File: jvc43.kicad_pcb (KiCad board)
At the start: 6 copper layers, 101.6 x 50.8 mm, 134 parts, among them J201 8P8C_LED_Shielded, J301 8P8C_LED_Shielded, J401 USB_C_Receptacle_USB2.0, U201 LAN8831, U301 LAN8831, U401 LTC3622*DE, X101 25 MHz

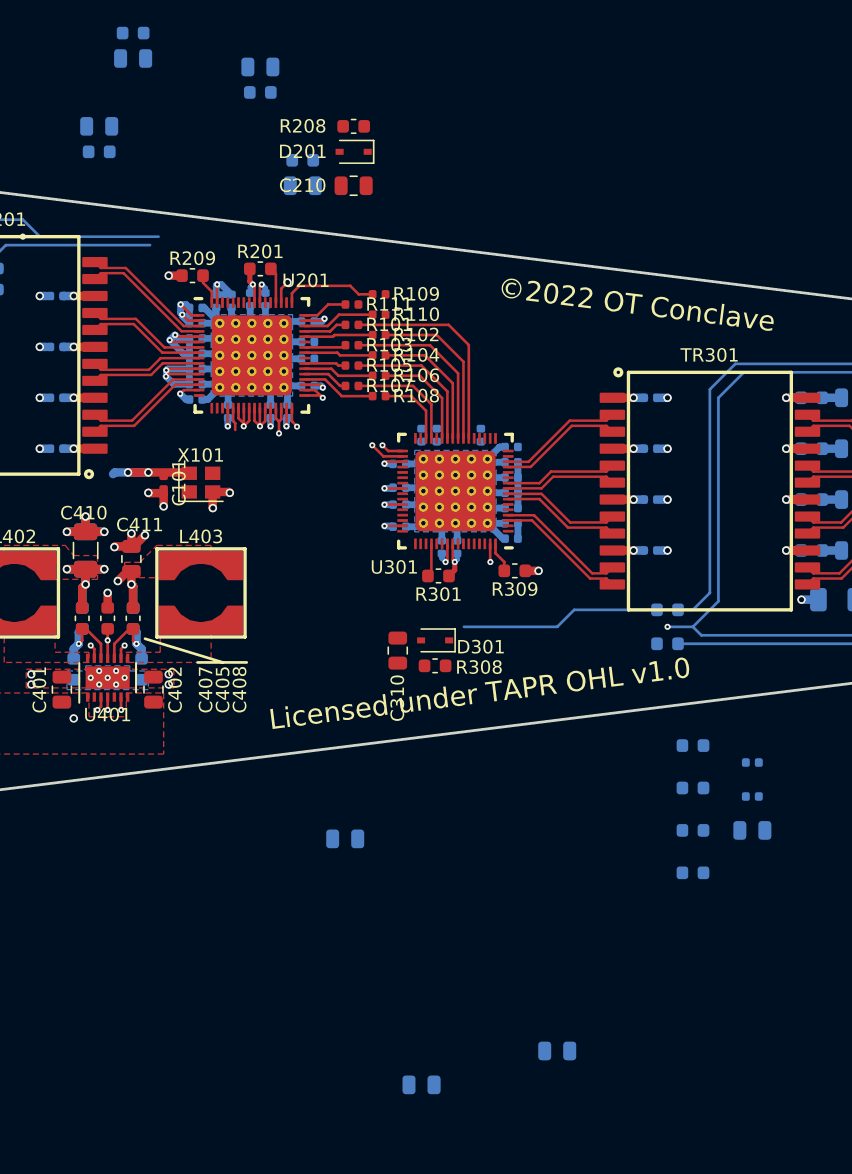
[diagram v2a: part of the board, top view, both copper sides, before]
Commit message: Routed the entire rest of the PHY1/2 bypass caps, inductors, and local power planes.  Had to move the oscillator to the right a bit to make way.
Also added a 50mil board edge keepout for components on the drawings layer.
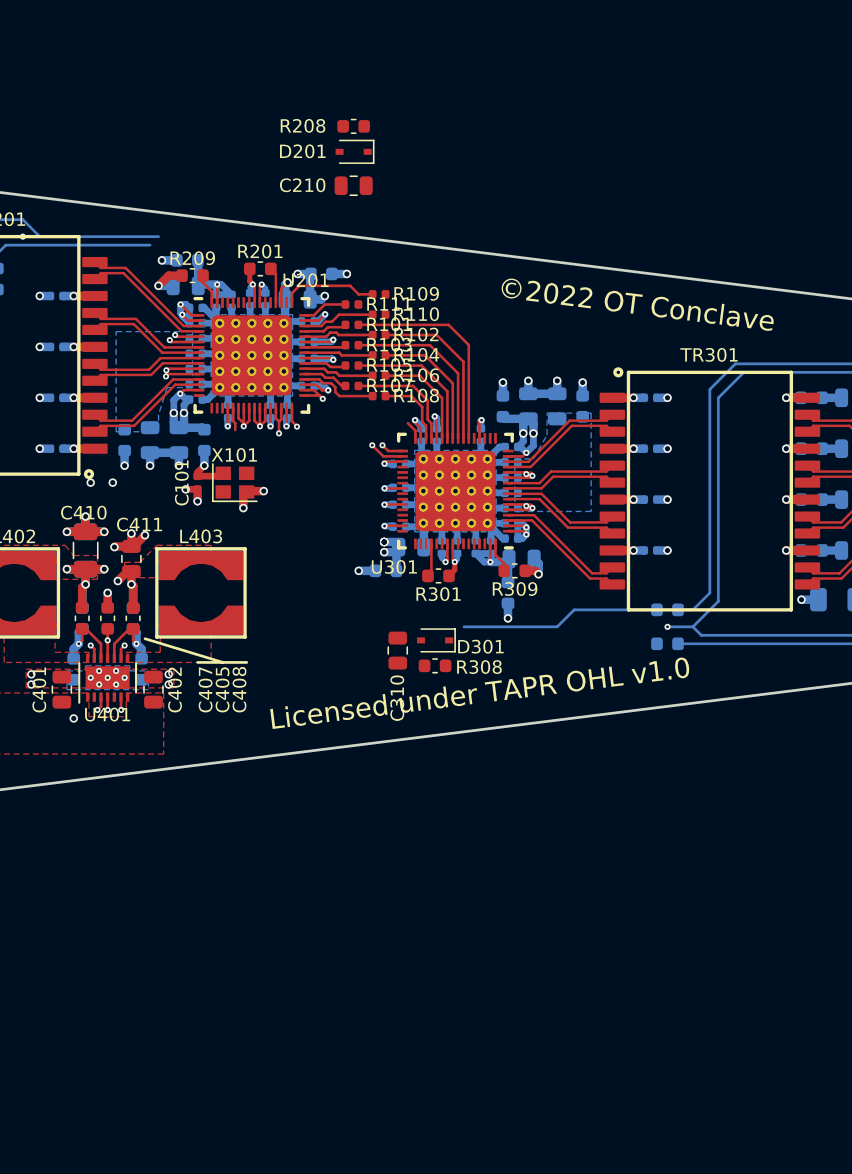
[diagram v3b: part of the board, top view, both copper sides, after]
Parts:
- moved C329 48.3 mm to (91.4, 44.5), turned to 90 degrees
- moved C319 40.3 mm to (80.5, 55.0)
- moved L301 37.7 mm to (87.4, 44.5), turned to 270 degrees
- moved C311 35.2 mm to (89.3, 44.5), turned to 90 degrees
- moved L303 32.8 mm to (93.3, 44.5), turned to 90 degrees
- moved L201 30.9 mm to (65.0, 47.0), turned to 90 degrees
- moved C211 28.8 mm to (63.1, 47.0), turned to 270 degrees
- moved C331 27.9 mm to (85.3, 55.0), turned to 90 degrees
- moved C332 26.7 mm to (88.8, 55.9)
- moved L302 26.4 mm to (78.6, 56.8), turned to 180 degrees
- moved C330 25.4 mm to (86.5, 55.0), turned to 90 degrees
- moved C229 23.8 mm to (61.0, 47.0), turned to 270 degrees
- moved L203 21.7 mm to (59.1, 47.0), turned to 270 degrees
- moved L304 20.1 mm to (87.8, 58.4), turned to 270 degrees
- moved C232 17.3 mm to (63.6, 35.4), turned to 180 degrees
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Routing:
- net GND: track 194.1 -> 214.3 mm, vias 45 -> 49
- net /Ethernet2/VDDAH: track 1.14 -> 15.9 mm, vias 0 -> 5
- net /Ethernet1/VDDAL: track 20.4 -> 9.15 mm
- net /Ethernet1/VDD: track 6.29 -> 15.1 mm, vias 3 -> 6
- net /Ethernet1/VDDAH: track 9.12 -> 16.4 mm, vias 3 -> 5
- net /Ethernet2/VDD: track 6.22 -> 13.3 mm, vias 3 -> 8
- net +1V1: track 11.6 -> 18.3 mm, vias 3 -> 9
- net /Ethernet2/VDDAL_PLL: track 1.37 -> 7.80 mm
- net +2V5: track 30.4 -> 36.7 mm, vias 11 -> 16
- net /Ethernet2/VDDAL: track 3.43 -> 7.81 mm, vias 0 -> 4
- net /Ethernet1/VDDAL_PLL: track 4.68 -> 8.06 mm
- net /ER_W2B: track 0.00 -> 1.36 mm
- added copper zone on L4.Cu, net /Ethernet1/VDD
- added copper zone on L4.Cu, net /Ethernet1/VDDAH
- added copper zone on B.Cu, net /Ethernet1/VDDAL
- added copper zone on L4.Cu, net /Ethernet2/VDD
- added copper zone on L4.Cu, net /Ethernet2/VDDAH
- added copper zone on B.Cu, net /Ethernet2/VDDAL

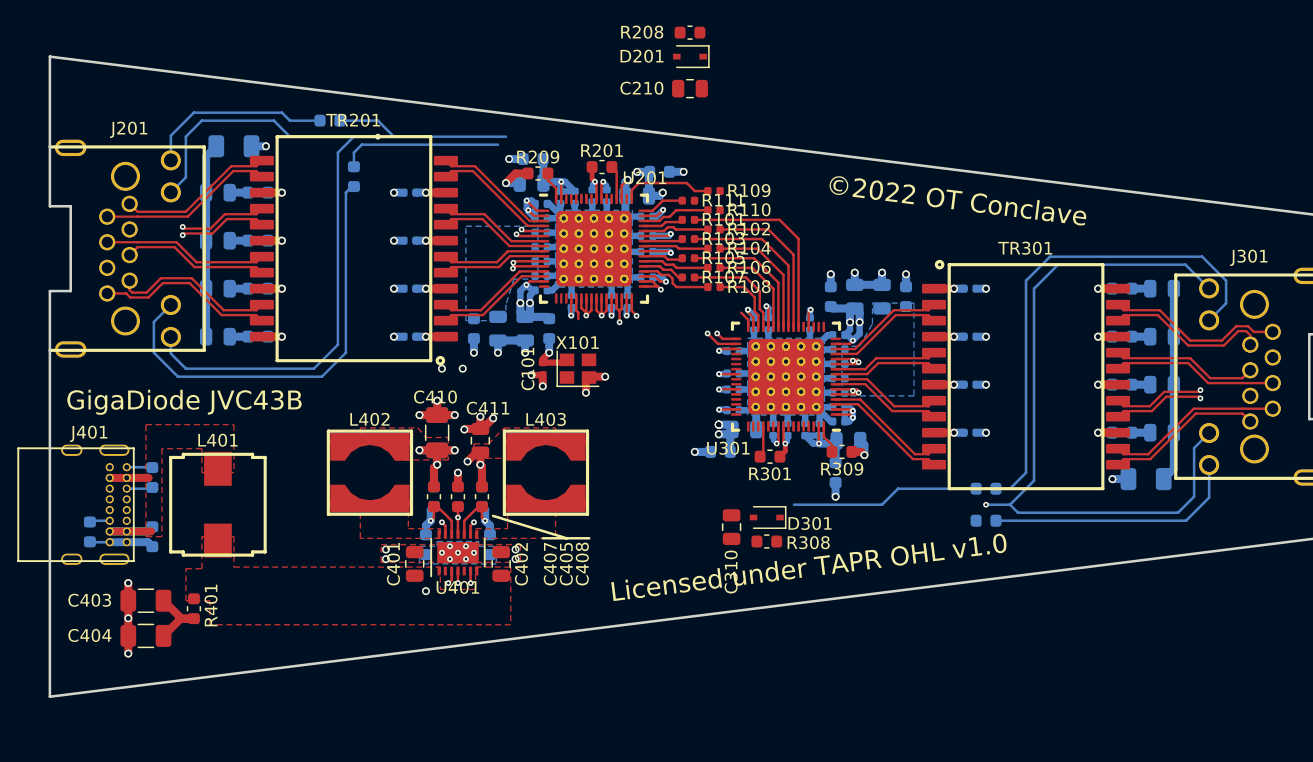
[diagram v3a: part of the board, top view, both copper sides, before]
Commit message: - Tweaked polygon shape of the two VDDAH slightly - Added fiducials (at the layout level, rather than schematic)
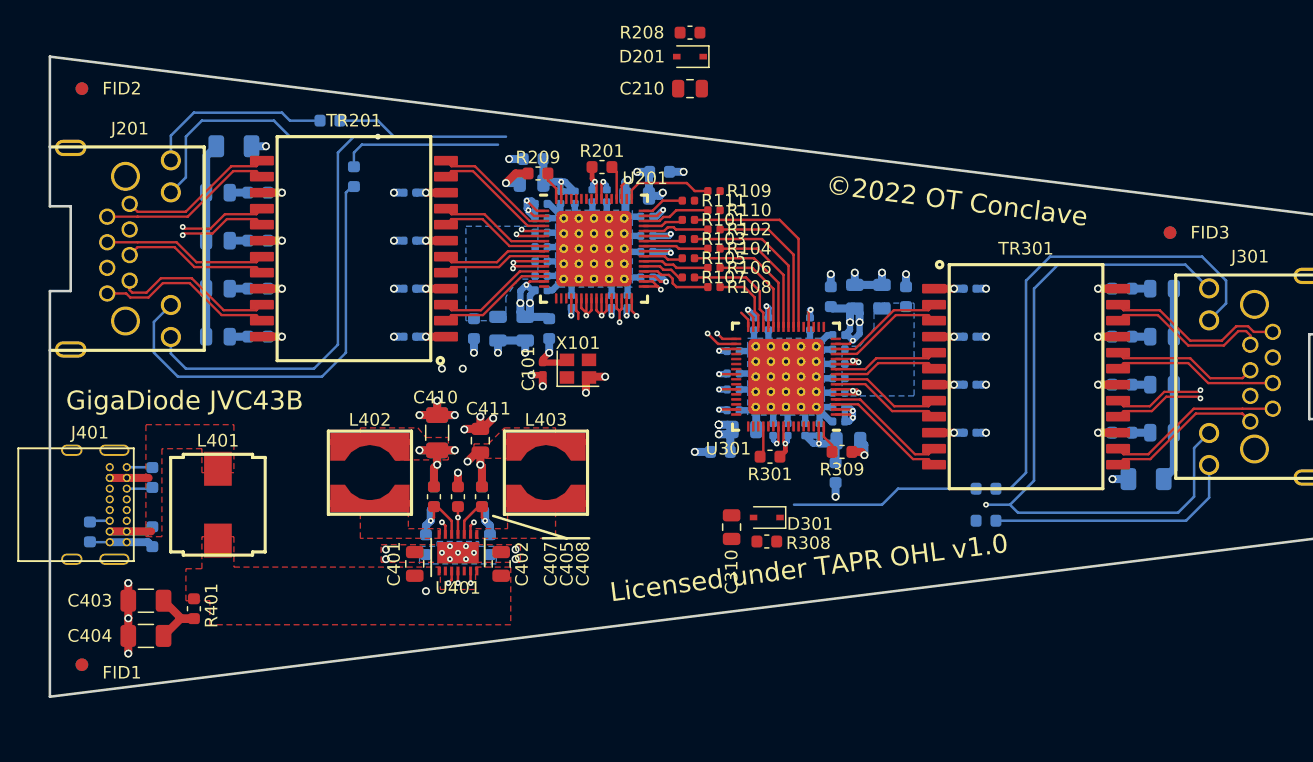
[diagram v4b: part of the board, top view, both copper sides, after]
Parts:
- added FID1: Fiducial_1mm_Dia_2mm_Outer, Fiducial:Fiducial_1mm_Dia_2mm_Outer, F.Cu at (27.9, 73.7)
- added FID2: Fiducial_1mm_Dia_2mm_Outer, Fiducial:Fiducial_1mm_Dia_2mm_Outer, F.Cu at (27.9, 27.9)
- added FID3: Fiducial_1mm_Dia_2mm_Outer, Fiducial:Fiducial_1mm_Dia_2mm_Outer, F.Cu at (114.3, 39.4)
- added FID4: Fiducial_1mm_Dia_2mm_Outer, Fiducial:Fiducial_1mm_Dia_2mm_Outer, B.Cu at (27.9, 73.7)
- added FID5: Fiducial_1mm_Dia_2mm_Outer, Fiducial:Fiducial_1mm_Dia_2mm_Outer, B.Cu at (27.9, 27.9)
- added FID6: Fiducial_1mm_Dia_2mm_Outer, Fiducial:Fiducial_1mm_Dia_2mm_Outer, B.Cu at (114.3, 39.4)
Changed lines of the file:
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@@
     (tracks 926)
     (zones 0)
-    (modules 134)
+    (modules 140)
     (nets 163)
   )
@@
     )
   )
+  (module Fiducial:Fiducial_1mm_Dia_2mm_Outer locked (layer F.Cu)
+    (at 27.94 73.66)
+    (descr "Circular Fiducial, 1mm bare copper top, 2mm keepout (Level A)")
+    (tags fiducial)
+    (attr smd)
+    (fp_text reference FID1 (at 3.175 0.635) (layer F.SilkS)
+      (effects (font (size 1 1) (thickness 0.15)))
+    )
+    (fp_text value Fiducial_1mm_Dia_2mm_Outer (at 0 2) (layer F.Fab)
+      (effects (font (size 1 1) (thickness 0.15)))
+    )
+    (fp_circle (center 0 0) (end 1.25 0) (layer F.CrtYd) (width 0.05))
+    (fp_text user %R (at 0 0) (layer F.Fab)
+      (effects (font (size 0.4 0.4) (thickness 0.06)))
+    )
+    (fp_circle (center 0 0) (end 1 0) (layer F.Fab) (width 0.1))
+    (pad "" smd circle (at 0 0) (size 1 1) (layers F.Cu F.Mask)
+      (solder_mask_margin 0.5) (clearance 0.5))
+  )
+  (module Fiducial:Fiducial_1mm_Dia_2mm_Outer locked (layer B.Cu)
+    (at 27.94 73.66)
+    (descr "Circular Fiducial, 1mm bare copper top, 2mm keepout (Level A)")
+    (tags fiducial)
+    (attr smd)
+    (fp_text reference FID4 (at 0 -1.905) (layer B.SilkS)
+      (effects (font (size 1 1) (thickness 0.15)) (justify mirror))
+    )
+    (fp_text value Fiducial_1mm_Dia_2mm_Outer (at 0 -2) (layer B.Fab)
+      (effects (font (size 1 1) (thickness 0.15)) (justify mirror))
+    )
+    (fp_circle (center 0 0) (end 1.25 0) (layer B.CrtYd) (width 0.05))
+    (fp_text user %R (at 0 0) (layer B.Fab)
+      (effects (font (size 0.4 0.4) (thickness 0.06)) (justify mirror))
+    )
+    (fp_circle (center 0 0) (end 1 0) (layer B.Fab) (width 0.1))
+    (pad "" smd circle (at 0 0) (size 1 1) (layers B.Cu B.Mask)
+      (solder_mask_margin 0.5) (clearance 0.5))
+  )
+  (module Fiducial:Fiducial_1mm_Dia_2mm_Outer locked (layer F.Cu)
+    (at 27.94 27.94)
+    (descr "Circular Fiducial, 1mm bare copper top, 2mm keepout (Level A)")
+    (tags fiducial)
+    (attr smd)
+    (fp_text reference FID2 (at 3.175 0) (layer F.SilkS)
+      (effects (font (size 1 1) (thickness 0.15)))
+    )
+    (fp_text value Fiducial_1mm_Dia_2mm_Outer (at 0 2) (layer F.Fab)
+      (effects (font (size 1 1) (thickness 0.15)))
+    )
+    (fp_circle (center 0 0) (end 1.25 0) (layer F.CrtYd) (width 0.05))
+    (fp_text user %R (at 0 0) (layer F.Fab)
+      (effects (font (size 0.4 0.4) (thickness 0.06)))
+    )
+    (fp_circle (center 0 0) (end 1 0) (layer F.Fab) (width 0.1))
+    (pad "" smd circle (at 0 0) (size 1 1) (layers F.Cu F.Mask)
+      (solder_mask_margin 0.5) (clearance 0.5))
+  )
+  (module Fiducial:Fiducial_1mm_Dia_2mm_Outer locked (layer B.Cu)
+    (at 27.94 27.94)
+    (descr "Circular Fiducial, 1mm bare copper top, 2mm keepout (Level A)")
+    (tags fiducial)
+    (attr smd)
+    (fp_text reference FID5 (at 0 2) (layer B.SilkS)
+      (effects (font (size 1 1) (thickness 0.15)) (justify mirror))
+    )
+    (fp_text value Fiducial_1mm_Dia_2mm_Outer (at 0 -2) (layer B.Fab)
+      (effects (font (size 1 1) (thickness 0.15)) (justify mirror))
+    )
+    (fp_circle (center 0 0) (end 1.25 0) (layer B.CrtYd) (width 0.05))
+    (fp_text user %R (at 0 0) (layer B.Fab)
+      (effects (font (size 0.4 0.4) (thickness 0.06)) (justify mirror))
+    )
+    (fp_circle (center 0 0) (end 1 0) (layer B.Fab) (width 0.1))
+    (pad "" smd circle (at 0 0) (size 1 1) (layers B.Cu B.Mask)
+      (solder_mask_margin 0.5) (clearance 0.5))
+  )
+  (module Fiducial:Fiducial_1mm_Dia_2mm_Outer locked (layer F.Cu)
+    (at 114.3 39.37)
+    (descr "Circular Fiducial, 1mm bare copper top, 2mm keepout (Level A)")
+    (tags fiducial)
+    (attr smd)
+    (fp_text reference FID3 (at 3.175 0) (layer F.SilkS)
+      (effects (font (size 1 1) (thickness 0.15)))
+    )
+    (fp_text value Fiducial_1mm_Dia_2mm_Outer (at 0 2) (layer F.Fab)
+      (effects (font (size 1 1) (thickness 0.15)))
+    )
+    (fp_circle (center 0 0) (end 1.25 0) (layer F.CrtYd) (width 0.05))
+    (fp_text user %R (at 0 0) (layer F.Fab)
+      (effects (font (size 0.4 0.4) (thickness 0.06)))
+    )
+    (fp_circle (center 0 0) (end 1 0) (layer F.Fab) (width 0.1))
+    (pad "" smd circle (at 0 0) (size 1 1) (layers F.Cu F.Mask)
+      (solder_mask_margin 0.5) (clearance 0.5))
+  )
+  (module Fiducial:Fiducial_1mm_Dia_2mm_Outer locked (layer B.Cu)
+    (at 114.3 39.37)
+    (descr "Circular Fiducial, 1mm bare copper top, 2mm keepout (Level A)")
+    (tags fiducial)
+    (attr smd)
+    (fp_text reference FID6 (at -3.175 0) (layer B.SilkS)
+      (effects (font (size 1 1) (thickness 0.15)) (justify mirror))
+    )
+    (fp_text value Fiducial_1mm_Dia_2mm_Outer (at 0 -2) (layer B.Fab)
+      (effects (font (size 1 1) (thickness 0.15)) (justify mirror))
+    )
+    (fp_circle (center 0 0) (end 1.25 0) (layer B.CrtYd) (width 0.05))
+    (fp_text user %R (at 0 0) (layer B.Fab)
+      (effects (font (size 0.4 0.4) (thickness 0.06)) (justify mirror))
+    )
+    (fp_circle (center 0 0) (end 1 0) (layer B.Fab) (width 0.1))
+    (pad "" smd circle (at 0 0) (size 1 1) (layers B.Cu B.Mask)
+      (solder_mask_margin 0.5) (clearance 0.5))
+  )
   (gr_line (start 26.67 74.93) (end 26.67 26.67) (layer Dwgs.User) (width 0.2))
   (gr_line (start 125.73 62.23) (end 26.67 74.93) (layer Dwgs.User) (width 0.2))
@@
     (polygon
       (pts
-        (xy 88.265 48.387) (xy 89.662 48.387) (xy 90.678 46.609) (xy 90.678 44.958) (xy 93.98 44.958)
+        (xy 88.265 48.387) (xy 89.662 48.387) (xy 90.805 46.99) (xy 90.805 44.958) (xy 93.98 44.958)
         (xy 93.98 52.324) (xy 88.265 52.324)
       )
@@
     (polygon
       (pts
-        (xy 58.42 46.355) (xy 58.42 38.862) (xy 64.135 38.862) (xy 64.135 43.053) (xy 62.23 43.053)
-        (xy 61.595 45.085) (xy 61.595 46.355)
+        (xy 58.42 46.355) (xy 58.42 38.862) (xy 64.135 38.862) (xy 64.135 43.053) (xy 62.611 43.053)
+        (xy 61.595 44.45) (xy 61.595 46.355)
       )
     )
